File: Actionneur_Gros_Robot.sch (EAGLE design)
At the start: 52 parts, among them M1 ARDUINO-NANO-3.0, M10 SERVO, M11 SERVO, M2 SERVO, M3 SERVO, M4 SERVO, M5 SERVO, M6 SERVO, M7 SERVO, M8 SERVO, M9 SERVO, Y1 16MHz

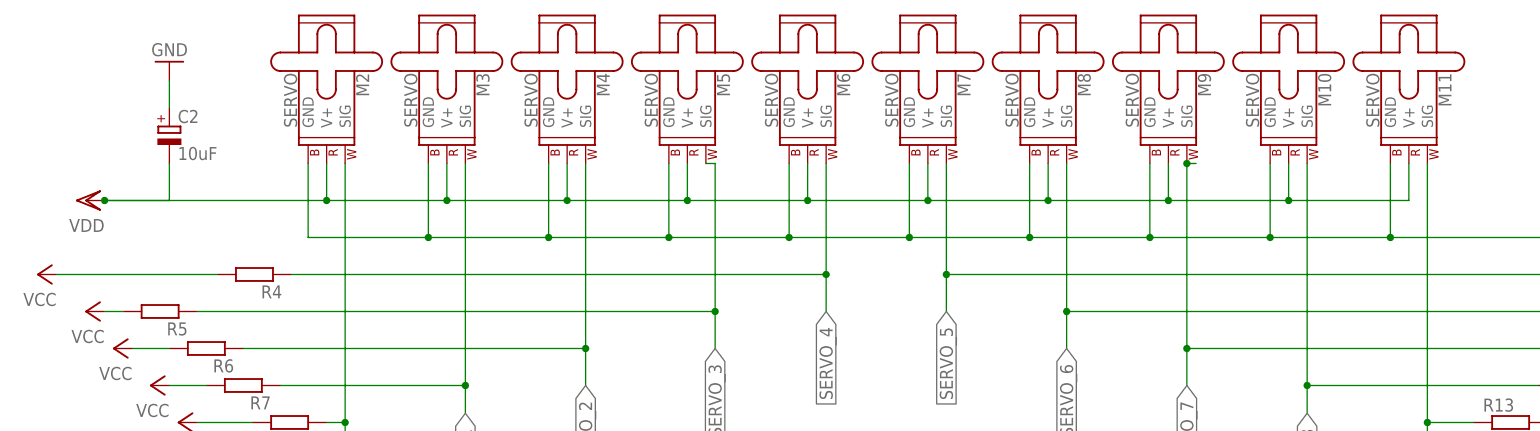
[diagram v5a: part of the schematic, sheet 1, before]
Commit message: Added CAM job
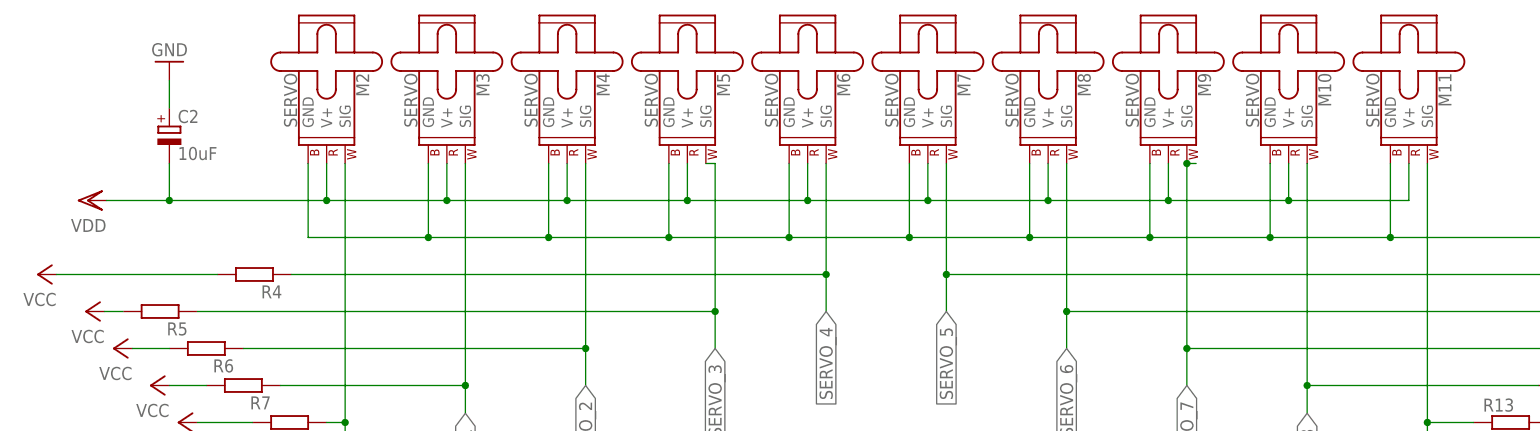
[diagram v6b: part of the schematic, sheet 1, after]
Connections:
- net VCC: no longer C2.-, M10.V+, M11.V+, M2.V+, M3.V+, M4.V+, M5.V+, M6.V+, M7.V+, M8.V+, M9.V+
- net VDD: now also C2.-, M10.V+, M11.V+, M2.V+, M3.V+, M4.V+, M5.V+, M6.V+, M7.V+, M8.V+, M9.V+
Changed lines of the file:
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@@
 <attribute name="VALUE" x="45.72" y="12.7" size="1.778" layer="96"/>
 </instance>
-<instance part="P+5" gate="G$1" x="15.24" y="148.59" smashed="yes" rot="R90">
-<attribute name="VALUE" x="17.78" y="146.05" size="1.778" layer="96" rot="R180"/>
+<instance part="P+5" gate="G$1" x="15.494" y="148.59" smashed="yes" rot="R90">
+<attribute name="VALUE" x="18.034" y="146.05" size="1.778" layer="96" rot="R180"/>
 </instance>
 <instance part="GND7" gate="1" x="222.25" y="167.64" smashed="yes" rot="R180">
@@
 </segment>
 <segment>
-<pinref part="P+5" gate="G$1" pin="VDD"/>
-<pinref part="M2" gate="G$1" pin="V+"/>
-<wire x1="48.26" y1="153.67" x2="48.26" y2="148.59" width="0.1524" layer="91"/>
-<wire x1="48.26" y1="148.59" x2="17.78" y2="148.59" width="0.1524" layer="91"/>
-<pinref part="M3" gate="G$1" pin="V+"/>
-<wire x1="64.77" y1="153.67" x2="64.77" y2="148.59" width="0.1524" layer="91"/>
-<wire x1="64.77" y1="148.59" x2="48.26" y2="148.59" width="0.1524" layer="91"/>
-<junction x="48.26" y="148.59"/>
-<pinref part="M4" gate="G$1" pin="V+"/>
-<wire x1="81.28" y1="153.67" x2="81.28" y2="148.59" width="0.1524" layer="91"/>
-<wire x1="81.28" y1="148.59" x2="64.77" y2="148.59" width="0.1524" layer="91"/>
-<junction x="64.77" y="148.59"/>
-<pinref part="M5" gate="G$1" pin="V+"/>
-<wire x1="97.79" y1="153.67" x2="97.79" y2="148.59" width="0.1524" layer="91"/>
-<wire x1="97.79" y1="148.59" x2="81.28" y2="148.59" width="0.1524" layer="91"/>
-<junction x="81.28" y="148.59"/>
-<pinref part="M6" gate="G$1" pin="V+"/>
-<wire x1="114.3" y1="153.67" x2="114.3" y2="148.59" width="0.1524" layer="91"/>
-<wire x1="114.3" y1="148.59" x2="97.79" y2="148.59" width="0.1524" layer="91"/>
-<junction x="97.79" y="148.59"/>
-<pinref part="M7" gate="G$1" pin="V+"/>
-<wire x1="130.81" y1="153.67" x2="130.81" y2="148.59" width="0.1524" layer="91"/>
-<wire x1="130.81" y1="148.59" x2="114.3" y2="148.59" width="0.1524" layer="91"/>
-<junction x="114.3" y="148.59"/>
-<pinref part="M8" gate="G$1" pin="V+"/>
-<wire x1="147.32" y1="153.67" x2="147.32" y2="148.59" width="0.1524" layer="91"/>
-<wire x1="147.32" y1="148.59" x2="130.81" y2="148.59" width="0.1524" layer="91"/>
-<junction x="130.81" y="148.59"/>
-<pinref part="M9" gate="G$1" pin="V+"/>
-<wire x1="163.83" y1="153.67" x2="163.83" y2="148.59" width="0.1524" layer="91"/>
-<wire x1="163.83" y1="148.59" x2="147.32" y2="148.59" width="0.1524" layer="91"/>
-<junction x="147.32" y="148.59"/>
-<pinref part="M10" gate="G$1" pin="V+"/>
-<wire x1="180.34" y1="153.67" x2="180.34" y2="148.59" width="0.1524" layer="91"/>
-<wire x1="180.34" y1="148.59" x2="163.83" y2="148.59" width="0.1524" layer="91"/>
-<junction x="163.83" y="148.59"/>
-<pinref part="M11" gate="G$1" pin="V+"/>
-<wire x1="196.85" y1="153.67" x2="196.85" y2="148.59" width="0.1524" layer="91"/>
-<wire x1="196.85" y1="148.59" x2="180.34" y2="148.59" width="0.1524" layer="91"/>
-<junction x="180.34" y="148.59"/>
-<pinref part="C2" gate="G$1" pin="-"/>
-<wire x1="26.67" y1="153.67" x2="26.67" y2="148.59" width="0.1524" layer="91"/>
-<wire x1="26.67" y1="148.59" x2="17.78" y2="148.59" width="0.1524" layer="91"/>
-<junction x="17.78" y="148.59"/>
-</segment>
-<segment>
 <pinref part="P+6" gate="VCC" pin="VCC"/>
 <pinref part="R4" gate="G$1" pin="2"/>
@@
 </segment>
 </net>
+<net name="VDD" class="0">
+<segment>
+<pinref part="C2" gate="G$1" pin="-"/>
+<wire x1="26.67" y1="153.67" x2="26.67" y2="148.59" width="0.1524" layer="91"/>
+<pinref part="P+5" gate="G$1" pin="VDD"/>
+<wire x1="18.034" y1="148.59" x2="26.67" y2="148.59" width="0.1524" layer="91"/>
+<pinref part="M2" gate="G$1" pin="V+"/>
+<wire x1="48.26" y1="153.67" x2="48.26" y2="148.59" width="0.1524" layer="91"/>
+<wire x1="26.67" y1="148.59" x2="48.26" y2="148.59" width="0.1524" layer="91"/>
+<junction x="26.67" y="148.59"/>
+<pinref part="M3" gate="G$1" pin="V+"/>
+<wire x1="64.77" y1="153.67" x2="64.77" y2="148.59" width="0.1524" layer="91"/>
+<wire x1="48.26" y1="148.59" x2="64.77" y2="148.59" width="0.1524" layer="91"/>
+<junction x="48.26" y="148.59"/>
+<pinref part="M4" gate="G$1" pin="V+"/>
+<wire x1="81.28" y1="153.67" x2="81.28" y2="148.59" width="0.1524" layer="91"/>
+<wire x1="64.77" y1="148.59" x2="81.28" y2="148.59" width="0.1524" layer="91"/>
+<junction x="64.77" y="148.59"/>
+<pinref part="M5" gate="G$1" pin="V+"/>
+<wire x1="97.79" y1="153.67" x2="97.79" y2="148.59" width="0.1524" layer="91"/>
+<wire x1="81.28" y1="148.59" x2="97.79" y2="148.59" width="0.1524" layer="91"/>
+<junction x="81.28" y="148.59"/>
+<pinref part="M6" gate="G$1" pin="V+"/>
+<wire x1="114.3" y1="153.67" x2="114.3" y2="148.59" width="0.1524" layer="91"/>
+<wire x1="97.79" y1="148.59" x2="114.3" y2="148.59" width="0.1524" layer="91"/>
+<junction x="97.79" y="148.59"/>
+<pinref part="M7" gate="G$1" pin="V+"/>
+<wire x1="130.81" y1="153.67" x2="130.81" y2="148.59" width="0.1524" layer="91"/>
+<wire x1="114.3" y1="148.59" x2="130.81" y2="148.59" width="0.1524" layer="91"/>
+<junction x="114.3" y="148.59"/>
+<pinref part="M8" gate="G$1" pin="V+"/>
+<wire x1="147.32" y1="153.67" x2="147.32" y2="148.59" width="0.1524" layer="91"/>
+<wire x1="130.81" y1="148.59" x2="147.32" y2="148.59" width="0.1524" layer="91"/>
+<junction x="130.81" y="148.59"/>
+<pinref part="M9" gate="G$1" pin="V+"/>
+<wire x1="163.83" y1="153.67" x2="163.83" y2="148.59" width="0.1524" layer="91"/>
+<wire x1="147.32" y1="148.59" x2="163.83" y2="148.59" width="0.1524" layer="91"/>
+<junction x="147.32" y="148.59"/>
+<pinref part="M10" gate="G$1" pin="V+"/>
+<wire x1="163.83" y1="148.59" x2="180.34" y2="148.59" width="0.1524" layer="91"/>
+<wire x1="180.34" y1="148.59" x2="180.34" y2="153.67" width="0.1524" layer="91"/>
+<junction x="163.83" y="148.59"/>
+<pinref part="M11" gate="G$1" pin="V+"/>
+<wire x1="196.85" y1="153.67" x2="196.85" y2="148.59" width="0.1524" layer="91"/>
+<wire x1="180.34" y1="148.59" x2="196.85" y2="148.59" width="0.1524" layer="91"/>
+<junction x="180.34" y="148.59"/>
+</segment>
+</net>

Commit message: revA02
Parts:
- C2: value 10uF -> 47uF
- R2: value (none) -> 10k
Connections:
- net GND: now also C2.-; no longer C2.+
- net VDD: now also C2.+; no longer C2.-
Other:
- moved on the sheet: C2
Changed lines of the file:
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@@
 <part name="C1" library="rcl" library_urn="urn:adsk.eagle:library:334" deviceset="C-EU" device="025-025X050" package3d_urn="urn:adsk.eagle:package:23629/2" value="100nF"/>
 <part name="GND4" library="supply1" library_urn="urn:adsk.eagle:library:371" deviceset="GND" device=""/>
-<part name="R2" library="rcl" library_urn="urn:adsk.eagle:library:334" deviceset="R-EU_" device="0204/7" package3d_urn="urn:adsk.eagle:package:23498/2"/>
+<part name="R2" library="rcl" library_urn="urn:adsk.eagle:library:334" deviceset="R-EU_" device="0204/7" package3d_urn="urn:adsk.eagle:package:23498/2" value="10k"/>
 <part name="R3" library="rcl" library_urn="urn:adsk.eagle:library:334" deviceset="R-EU_" device="0204/7" package3d_urn="urn:adsk.eagle:package:23498/2"/>
 <part name="P+2" library="supply1" library_urn="urn:adsk.eagle:library:371" deviceset="VCC" device=""/>
@@
 <part name="VDD9" library="supply1" library_urn="urn:adsk.eagle:library:371" deviceset="VDD" device=""/>
 <part name="GND17" library="supply1" library_urn="urn:adsk.eagle:library:371" deviceset="GND" device=""/>
-<part name="C2" library="rcl" library_urn="urn:adsk.eagle:library:334" deviceset="CPOL-EU" device="E2.5-7" package3d_urn="urn:adsk.eagle:package:23345/1" value="10uF"/>
+<part name="C2" library="rcl" library_urn="urn:adsk.eagle:library:334" deviceset="CPOL-EU" device="E2.5-7" package3d_urn="urn:adsk.eagle:package:23345/1" value="47uF"/>
 <part name="C5" library="rcl" library_urn="urn:adsk.eagle:library:334" deviceset="C-EU" device="025-025X050" package3d_urn="urn:adsk.eagle:package:23629/2" value="100nF"/>
 <part name="VDD10" library="supply1" library_urn="urn:adsk.eagle:library:371" deviceset="VDD" device=""/>
@@
 <attribute name="VALUE" x="37.48" y="88.322" size="1.778" layer="96"/>
 </instance>
-<instance part="C2" gate="G$1" x="26.67" y="158.75" smashed="yes">
-<attribute name="NAME" x="27.813" y="159.2326" size="1.778" layer="95"/>
-<attribute name="VALUE" x="27.813" y="154.1526" size="1.778" layer="96"/>
+<instance part="C2" gate="G$1" x="26.67" y="157.734" smashed="yes" rot="R180">
+<attribute name="NAME" x="25.527" y="157.2514" size="1.778" layer="95" rot="R180"/>
+<attribute name="VALUE" x="25.527" y="162.3314" size="1.778" layer="96" rot="R180"/>
 </instance>
 <instance part="P+4" gate="VCC" x="104.394" y="92.456" smashed="yes">
@@
 </segment>
 <segment>
-<pinref part="C2" gate="G$1" pin="+"/>
 <pinref part="GND8" gate="1" pin="GND"/>
-<wire x1="26.67" y1="161.29" x2="26.67" y2="165.1" width="0.1524" layer="91"/>
+<pinref part="C2" gate="G$1" pin="-"/>
+<wire x1="26.67" y1="165.1" x2="26.67" y2="162.814" width="0.1524" layer="91"/>
 </segment>
 </net>
@@
 <net name="VDD" class="0">
 <segment>
-<pinref part="C2" gate="G$1" pin="-"/>
-<wire x1="26.67" y1="153.67" x2="26.67" y2="148.59" width="0.1524" layer="91"/>
 <pinref part="P+5" gate="G$1" pin="VDD"/>
-<wire x1="18.034" y1="148.59" x2="26.67" y2="148.59" width="0.1524" layer="91"/>
 <pinref part="M2" gate="G$1" pin="V+"/>
 <wire x1="48.26" y1="153.67" x2="48.26" y2="148.59" width="0.1524" layer="91"/>
-<wire x1="26.67" y1="148.59" x2="48.26" y2="148.59" width="0.1524" layer="91"/>
-<junction x="26.67" y="148.59"/>
+<wire x1="18.034" y1="148.59" x2="48.26" y2="148.59" width="0.1524" layer="91"/>
 <pinref part="M3" gate="G$1" pin="V+"/>
 <wire x1="64.77" y1="153.67" x2="64.77" y2="148.59" width="0.1524" layer="91"/>
@@
 <wire x1="180.34" y1="148.59" x2="196.85" y2="148.59" width="0.1524" layer="91"/>
 <junction x="180.34" y="148.59"/>
-</segment>
-</net>
+<pinref part="C2" gate="G$1" pin="+"/>
+<wire x1="26.67" y1="155.194" x2="26.67" y2="148.59" width="0.1524" layer="91"/>
+<wire x1="26.67" y1="148.59" x2="18.034" y2="148.59" width="0.1524" layer="91"/>
+<junction x="18.034" y="148.59"/>
+</segment>
+</net>

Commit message: revA2
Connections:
- net VCC: now also J3.17, J3.18; no longer J3.21, J3.22
- net VDD: now also J3.21, J3.22; no longer J3.17, J3.18
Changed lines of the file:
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@@
-</segment>
-<segment>
-<pinref part="VDD4" gate="G$1" pin="VDD"/>
-<pinref part="J3" gate="G$1" pin="18"/>
-<wire x1="26.5" y1="43.96" x2="26.5" y2="42.46" width="0.1524" layer="91"/>
-<wire x1="26.5" y1="42.46" x2="40.42" y2="42.46" width="0.1524" layer="91"/>
-<pinref part="J3" gate="G$1" pin="17"/>
-<wire x1="40.42" y1="42.46" x2="50.58" y2="42.46" width="0.1524" layer="91"/>
-<junction x="40.42" y="42.46"/>
 </segment>
 <segment>
@@
 <wire x1="176.416" y1="151.336" x2="176.416" y2="147.066" width="0.1524" layer="91"/>
 <wire x1="176.416" y1="147.066" x2="176.53" y2="147.066" width="0.1524" layer="91"/>
+</segment>
+<segment>
+<pinref part="J3" gate="G$1" pin="22"/>
+<pinref part="J3" gate="G$1" pin="21"/>
+<wire x1="40.42" y1="37.38" x2="50.58" y2="37.38" width="0.1524" layer="91"/>
+<pinref part="VDD4" gate="G$1" pin="VDD"/>
+<wire x1="26.5" y1="43.96" x2="26.5" y2="37.38" width="0.1524" layer="91"/>
+<wire x1="26.5" y1="37.38" x2="40.42" y2="37.38" width="0.1524" layer="91"/>
+<junction x="40.42" y="37.38"/>
 </segment>
 </net>
@@
 <net name="VCC" class="0">
 <segment>
-<pinref part="J3" gate="G$1" pin="22"/>
-<pinref part="J3" gate="G$1" pin="21"/>
-<wire x1="40.42" y1="37.38" x2="50.58" y2="37.38" width="0.1524" layer="91"/>
-<pinref part="P+17" gate="VCC" pin="VCC"/>
-<wire x1="19.304" y1="44.704" x2="19.304" y2="37.38" width="0.1524" layer="91"/>
-<wire x1="19.304" y1="37.38" x2="40.42" y2="37.38" width="0.1524" layer="91"/>
-<junction x="40.42" y="37.38"/>
-</segment>
-<segment>
 <pinref part="P+18" gate="VCC" pin="VCC"/>
 <pinref part="SV4" gate="1" pin="6"/>
@@
 <wire x1="12.332" y1="59.182" x2="12.332" y2="44.582" width="0.1524" layer="91"/>
 </segment>
-</net>
+<segment>
+<pinref part="J3" gate="G$1" pin="18"/>
+<pinref part="J3" gate="G$1" pin="17"/>
+<wire x1="40.42" y1="42.46" x2="50.58" y2="42.46" width="0.1524" layer="91"/>
+<pinref part="P+17" gate="VCC" pin="VCC"/>
+<wire x1="19.304" y1="44.704" x2="19.304" y2="42.46" width="0.1524" layer="91"/>
+<wire x1="19.304" y1="42.46" x2="40.42" y2="42.46" width="0.1524" layer="91"/>
+<junction x="40.42" y="42.46"/>
+</segment>
+</net>
